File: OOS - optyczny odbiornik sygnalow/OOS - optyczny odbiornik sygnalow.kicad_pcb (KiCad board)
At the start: 2 copper layers, 72 x 79.5 mm, 127 parts, among them J1 Conn_01x02_Pin, J4 Conn_01x02_Socket, J5 Conn_Coaxial, J6 USB_C_Receptacle, Q1 SI2301CDS-T1-GE3, Q2 AOSS32334C, Q3 AOSS32334C, SW1 SW_Rotary_1x8_MP, U1 OPA300AIDBVR, U2 OPA300AIDBVR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

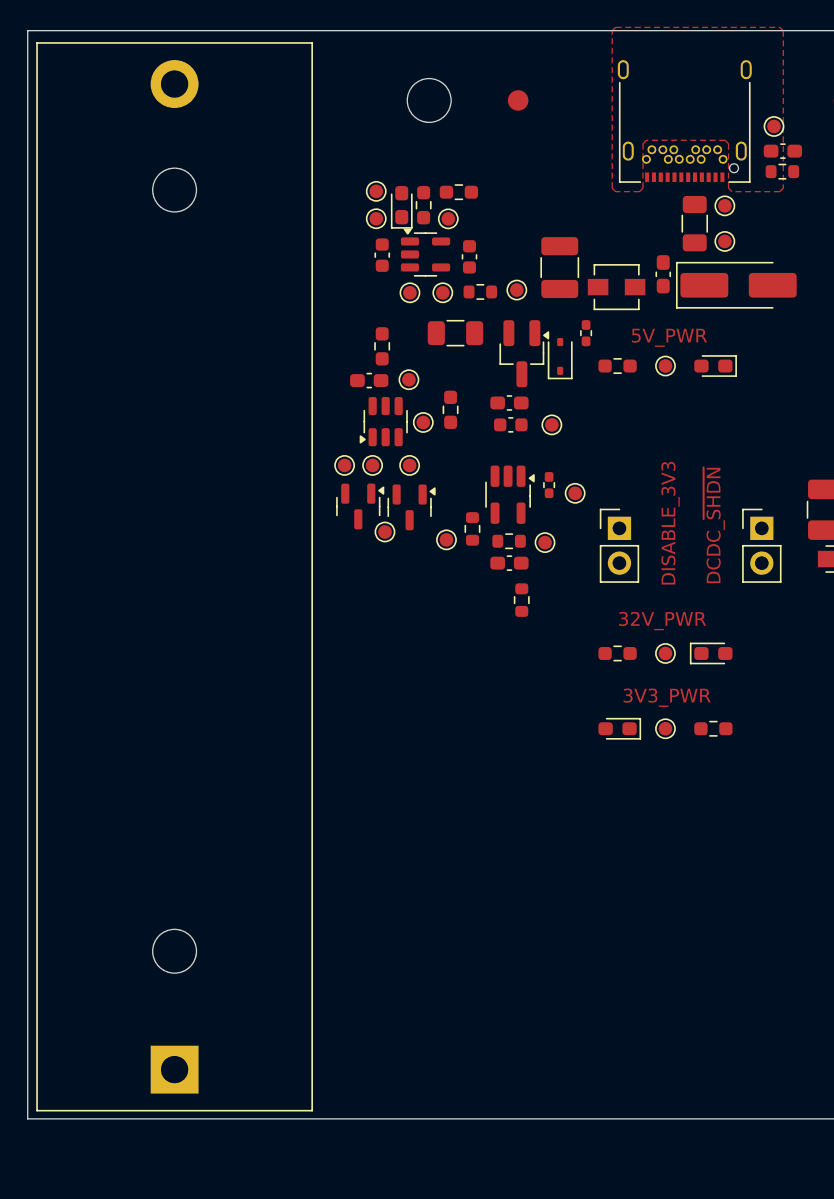
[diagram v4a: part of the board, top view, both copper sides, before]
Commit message: Change on charger side, moved components and place tracks and vias
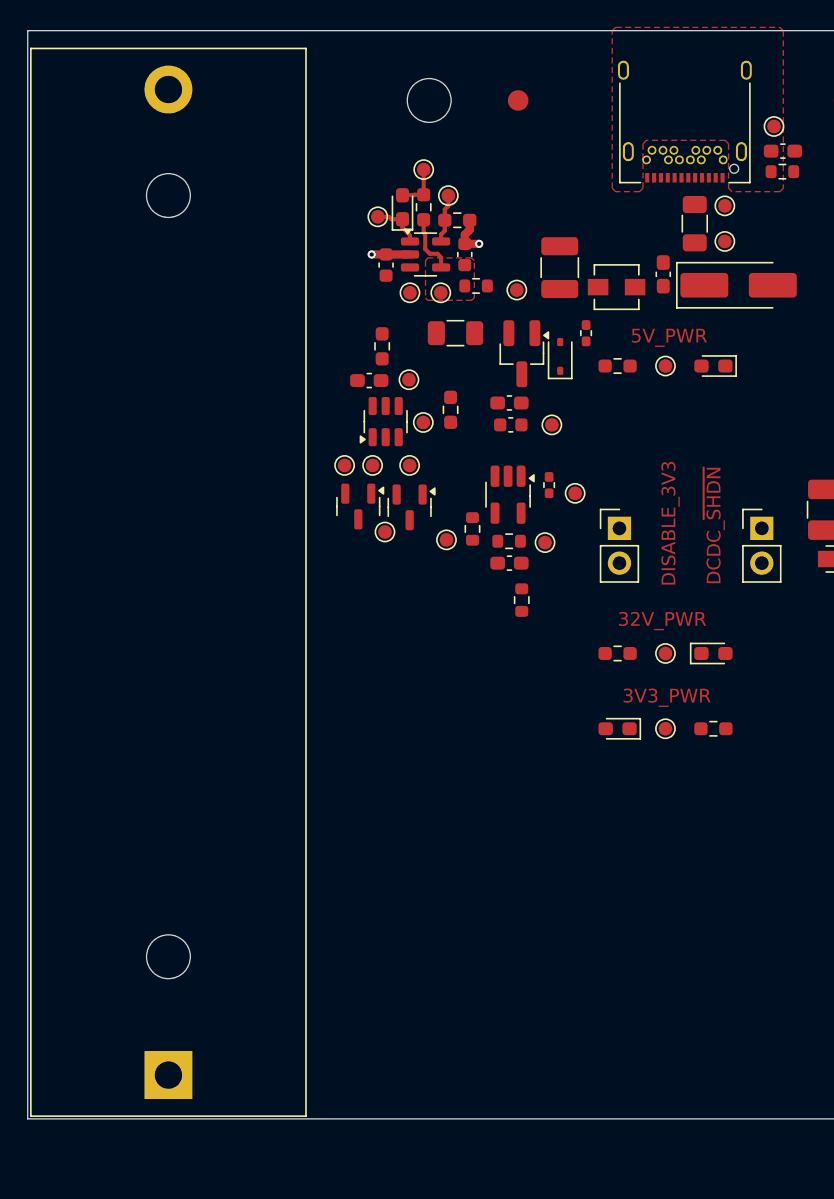
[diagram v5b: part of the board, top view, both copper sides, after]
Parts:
- moved TP19 3.81 mm to (224.2, 40.0)
- moved R20 2.05 mm to (226.7, 43.7)
- moved TP22 1.70 mm to (226.0, 41.9)
- moved C19 0.78 mm to (221.5, 47.0)
- moved BT1 0.60 mm to (205.6, 106.2)
- moved R25 0.54 mm to (228.0, 48.5)
- moved C18 0.39 mm to (227.2, 46.2)
- moved TP20 0.18 mm to (220.9, 43.5)
- moved D6 0.16 mm to (222.7, 42.8)
- moved R19 0.15 mm to (224.2, 42.8)
- moved TP18 0.15 mm to (225.5, 49.0)
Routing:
- net 0V: track 0.00 -> 5.72 mm, vias 0 -> 2
- net /Sekcja_Li-ion_Ladowanie/U3_V_{DD}: track 0.00 -> 4.34 mm
- net /Sekcja_Li-ion_Ladowanie/U3_STAT: track 0.00 -> 3.72 mm
- net /Sekcja_Li-ion_Ladowanie/U3_PROG: track 0.00 -> 3.57 mm
- net /Sekcja_Li-ion_Ladowanie/D5_A: track 0.00 -> 3.40 mm
- added copper zone on F.Cu, net /Sekcja_Li-ion_Ladowanie/U3_V_{DD}

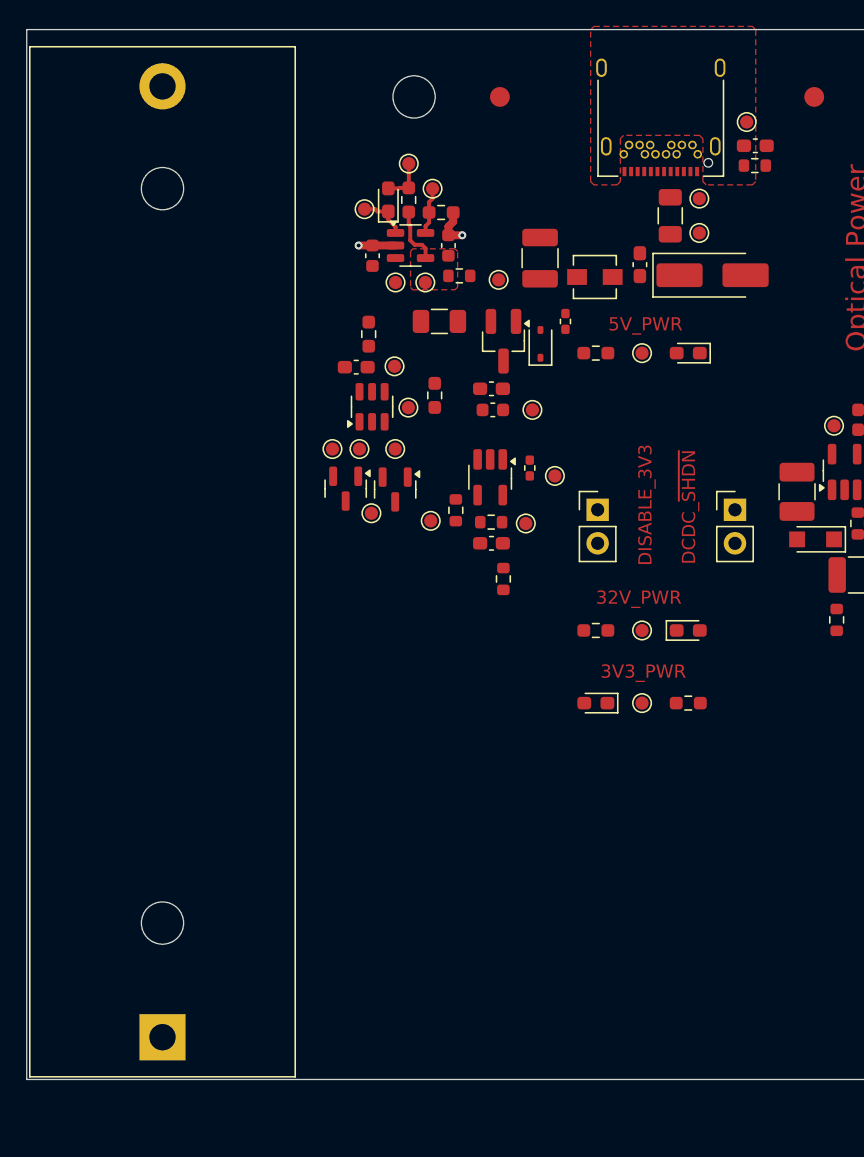
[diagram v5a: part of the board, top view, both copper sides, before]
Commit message: Place, route, adjust tracks and components for charger and balancer, create groups
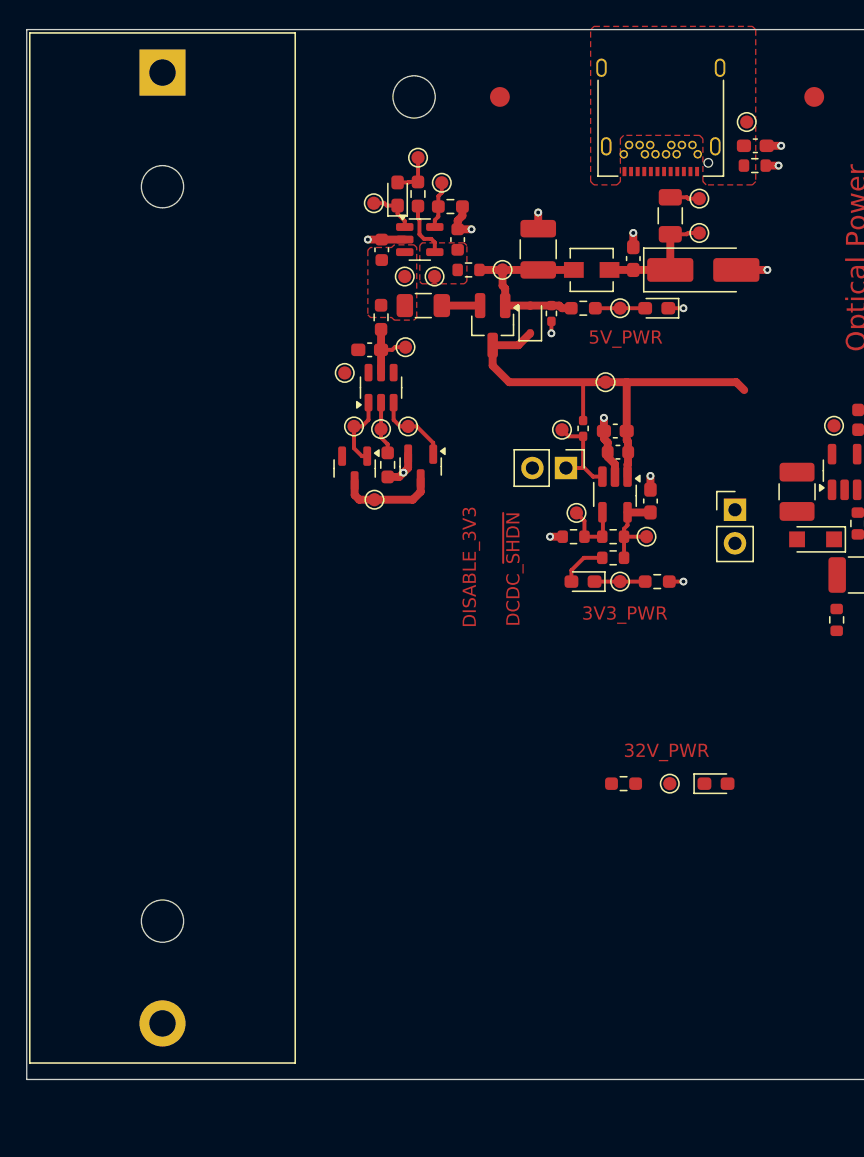
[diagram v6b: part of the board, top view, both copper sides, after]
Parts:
- moved BT1 73.0 mm to (205.6, 33.1), turned to -90 degrees
- moved C22 12.5 mm to (242.5, 65.6), turned to 90 degrees
- moved D1 11.8 mm to (247.5, 87.0)
- moved R1 11.8 mm to (240.5, 87.0)
- moved TP17 11.8 mm to (244.0, 87.0)
- moved TP31 11.1 mm to (236.9, 66.5)
- moved C20 10.0 mm to (240.1, 61.9)
- moved C17 9.91 mm to (239.9, 60.3)
- moved U6 9.54 mm to (239.8, 65.1)
- moved R2 9.50 mm to (243.0, 71.7)
- moved TP33 9.35 mm to (240.2, 71.7)
- moved R23 9.30 mm to (239.7, 68.3)
- moved D2 9.25 mm to (237.4, 71.7)
- moved TP32 9.19 mm to (242.2, 68.3)
- moved R24 9.13 mm to (236.7, 68.3), turned to 180 degrees
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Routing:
- net +V_DCDC_BOOST: track 0.00 -> 34.7 mm
- net 0V: track 5.72 -> 25.2 mm, vias 2 -> 14
- net +5V: track 0.00 -> 15.0 mm
- net /Sekcja_USB/C24_net: track 0.00 -> 9.54 mm
- net /Sekcja_Li-ion_Ladowanie/Q2/Q3_D: track 0.00 -> 7.44 mm
- net /Sekcja_Li-ion_Ladowanie/U6_EN: track 0.00 -> 7.22 mm
- net Net-(U6-V_{OUT}): track 0.00 -> 7.00 mm
- net /Sekcja_Li-ion_Ladowanie/U5_CO: track 0.00 -> 5.87 mm
- net /Sekcja_Li-ion_Ladowanie/U5_DO: track 0.00 -> 5.51 mm
- net /Sekcja_Li-ion_Ladowanie/U6_ADJ: track 0.00 -> 5.31 mm
- net /Sekcja_Li-ion_Ladowanie/U5_V_{DD}: track 0.00 -> 5.21 mm
- net /Sekcja_Li-ion_Ladowanie/U5_VM: track 0.00 -> 4.01 mm
- net Net-(D2-K): track 0.00 -> 3.84 mm
- net Net-(D8-A): track 0.00 -> 3.78 mm
- net +3V3: track 0.00 -> 3.58 mm
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- added copper zone on F.Cu, net +BAT

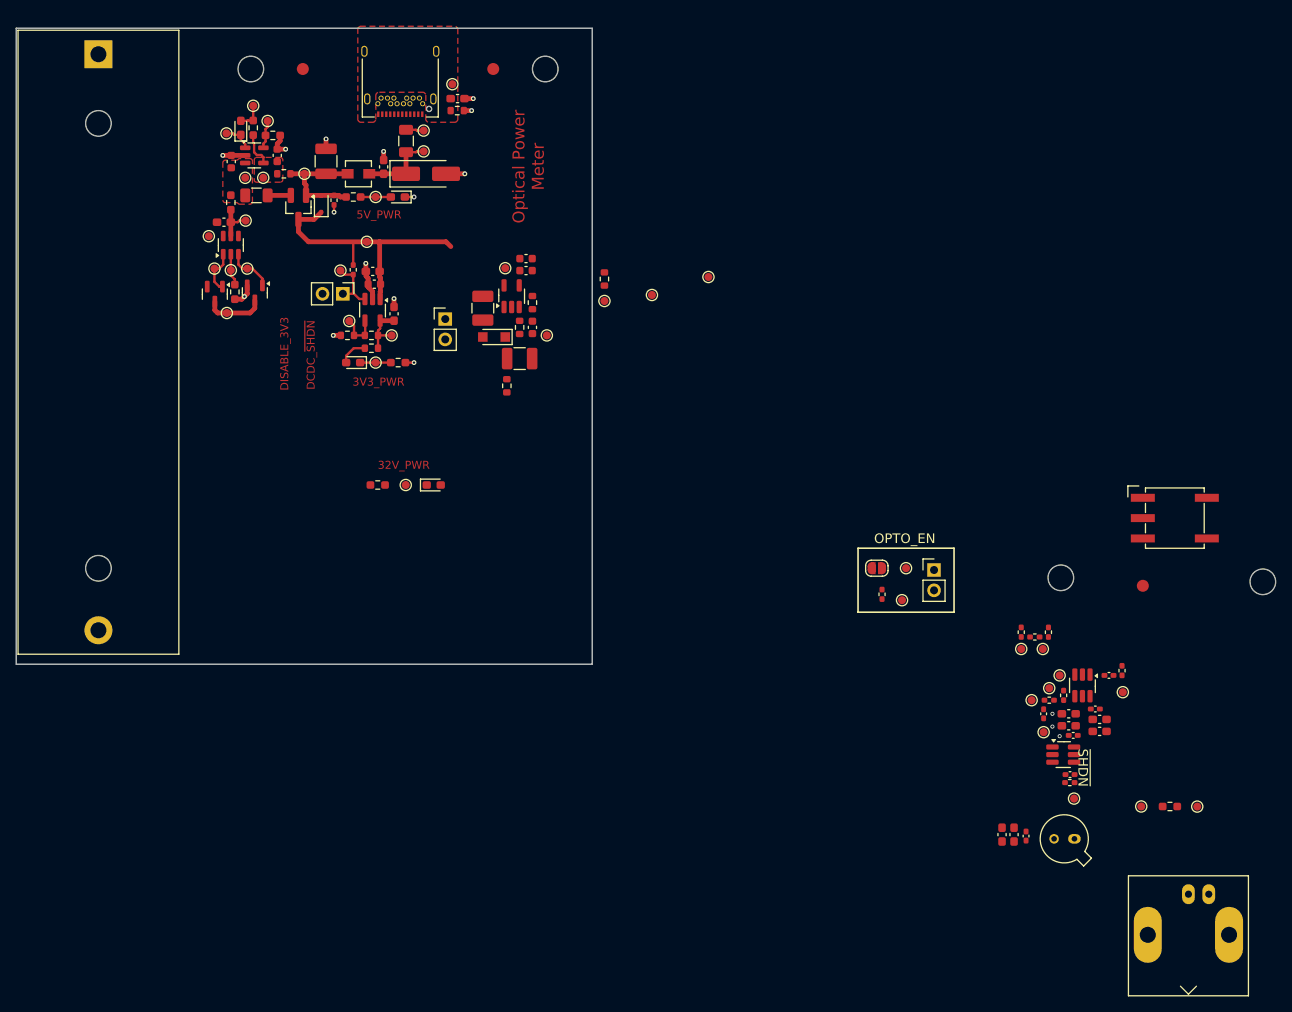
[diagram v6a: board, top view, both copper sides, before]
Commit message: Zrobiono placement oraz routing. Nalezy jeszcze dodac przelotki do gnd blisko pinow na top layer
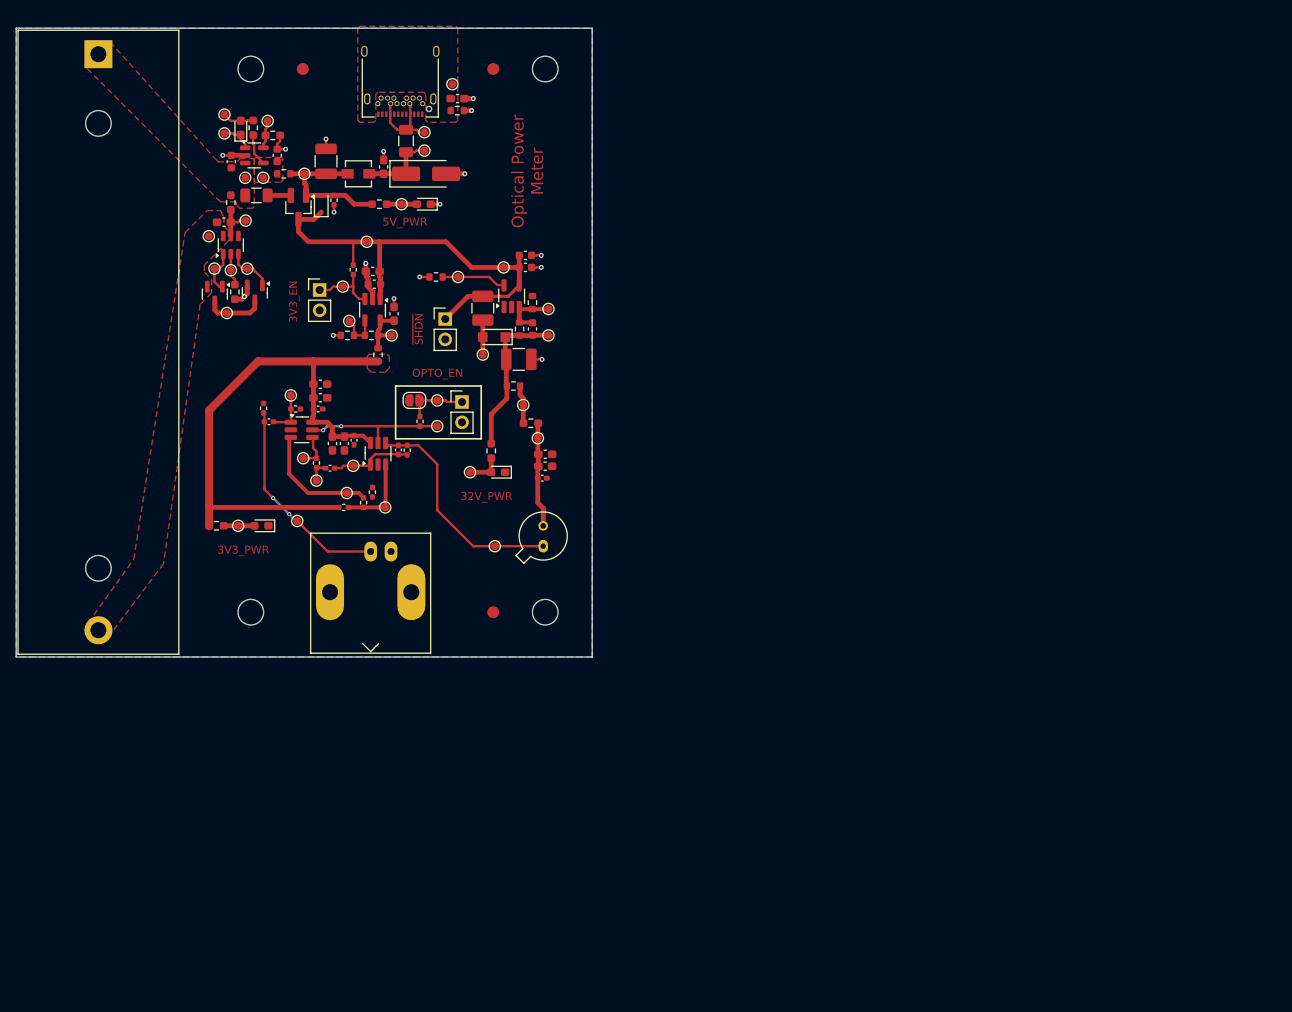
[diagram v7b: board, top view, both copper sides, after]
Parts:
- removed R10: 1k, Resistor_SMD:R_0402_1005Metric_Pad0.72x0.64mm_HandSolder
- removed SW1: SW_Rotary_1x8_MP, Button_Switch_SMD:Nidec_Copal_SH-7040B
- added R28: 1k, Resistor_SMD:R_0402_1005Metric_Pad0.72x0.64mm_HandSolder, F.Cu at (230.2, 77.5)
- moved R11 112.2 mm to (226.2, 77.4)
- moved J5 110.8 mm to (239.6, 95.3)
- moved C12 109.7 mm to (226.9, 79.1), turned to 180 degrees
- moved C2 106.6 mm to (233.3, 74.4)
- moved TP11 105.4 mm to (230.4, 91.5)
- moved C4 105.4 mm to (233.3, 76.1)
- moved C6 104.1 mm to (233.0, 77.5)
- moved U2 102.7 mm to (231.0, 80.1), turned to 0 degrees
- moved TP10 102.3 mm to (229.6, 75.8), turned to -90 degrees
- moved H3 101.3 mm to (224.6, 102.9)
- moved TP1 98.1 mm to (258.7, 77.0), turned to 90 degrees
- moved C1 98.0 mm to (234.8, 81.8), turned to -90 degrees
- moved TP9 97.6 mm to (231.2, 83.6), turned to -90 degrees
- moved C5 97.2 mm to (237.5, 81.4), turned to -90 degrees
- moved C3 97.2 mm to (236.3, 81.8), turned to -90 degrees
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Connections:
- D1 pad 1: Net-(D1-K) -> 0V
- D1 pad 2: +32V -> Net-(D1-A)
- D2 pad 1: Net-(D2-K) -> 0V
- D2 pad 2: +3V3 -> Net-(D2-A)
- R1 pad 1: Net-(D1-K) -> Net-(D4-K)
- R1 pad 2: 0V -> Net-(D1-A)
- R2 pad 1: Net-(D2-K) -> +3V3
- R2 pad 2: 0V -> Net-(D2-A)
- TP17 pad 1: Net-(D1-K) -> Net-(D1-A)
- TP33 pad 1: Net-(D2-K) -> Net-(D2-A)
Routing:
- net +3V3: track 3.58 -> 71.4 mm
- net /Sekcja_Analogowa/U1_TIA_-: track 0.00 -> 28.4 mm
- net /Sekcja_Analogowa/U2_x10_Out_AC: track 0.00 -> 25.8 mm, vias 0 -> 2
- net +V_DCDC_BOOST: track 34.7 -> 58.9 mm
- net Net-(D4-K): track 0.00 -> 19.8 mm
- net /Sekcja_Analogowa/U1/U2_En: track 0.00 -> 17.9 mm, vias 0 -> 2
- net /Sekcja_Analogowa/U2_x10_+: track 0.00 -> 15.0 mm
- net /Sekcja_Analogowa/D3_Cathode: track 0.00 -> 13.2 mm
- net /Sekcja_Analogowa/U1_TIA_Out: track 0.08 -> 10.1 mm
- net /Sekcja_Analogowa/U1_TIA_+: track 0.00 -> 9.97 mm
- net /Sekcja_USB/J6_Vbus: track 2.24 -> 10.7 mm
- net /Sekcja_DCDC_Boost/U3_~{SHDN}: track 0.00 -> 8.11 mm
- net /Sekcja_Analogowa/U1/U2_En_Alt_Con: track 0.00 -> 7.43 mm
- net /Sekcja_DCDC_Boost/U3_FB: track 0.00 -> 7.14 mm
- net /Sekcja_Analogowa/U2_x10_Out: track 0.00 -> 5.54 mm
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- added copper zone on F.Cu, net +3V3
- added copper zone on F.Cu, net -BAT
- added copper zone on B.Cu, net 0V
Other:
- board size 72 x 79.5 mm -> 72 x 78.6 mm
- board text added: "3V3_EN"
- board text removed: "DCDC_~{SHDN}"
- board text removed: "DISABLE_3V3"
- board text removed: "Rotary switch here"
- board text removed: "TODO: - !! Connect rotary switch (SW1) !! - place the 4th MH"
